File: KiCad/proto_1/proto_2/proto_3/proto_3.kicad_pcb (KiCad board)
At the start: 2 copper layers, 11 parts

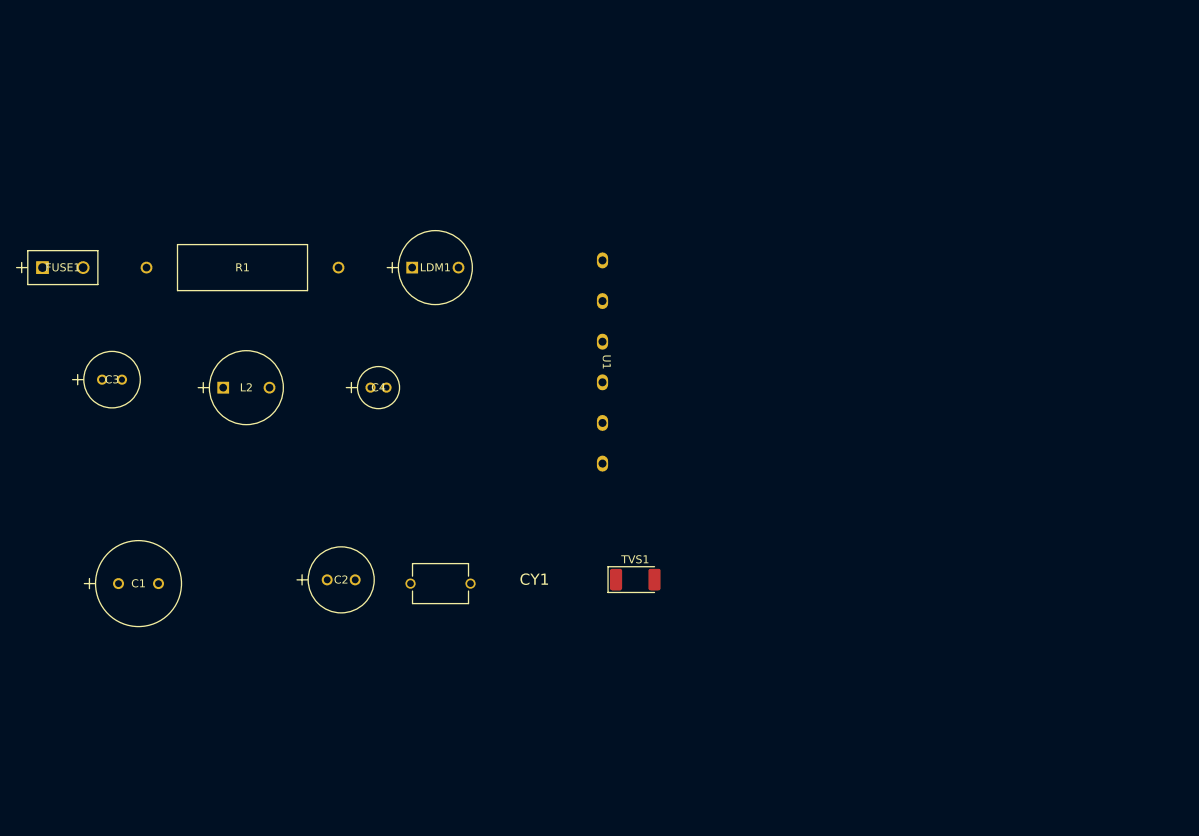
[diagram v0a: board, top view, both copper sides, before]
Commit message: Added through-holes for 120v source, moved components around on pcb
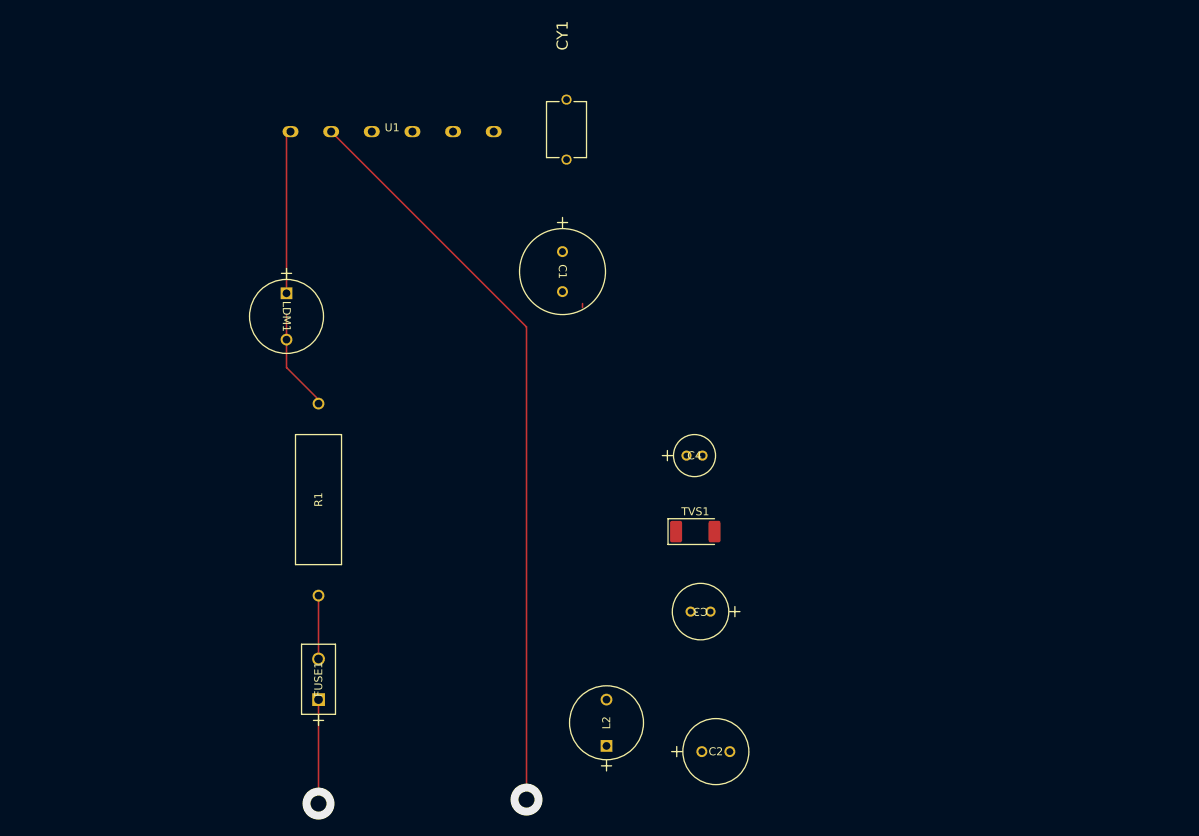
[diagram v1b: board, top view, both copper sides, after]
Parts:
- moved C3 81.4 mm to (157.5, 120.0), turned to 180 degrees
- moved C1 69.3 mm to (139.0, 75.0), turned to -90 degrees
- moved L2 65.6 mm to (144.5, 136.8), turned to 90 degrees
- moved FUSE1 64.1 mm to (108.5, 131.0), turned to 90 degrees
- moved CY1 58.9 mm to (139.5, 59.8), turned to 90 degrees
- moved C2 51.5 mm to (156.4, 137.5)
- moved R1 46.3 mm to (108.5, 118.0), turned to 90 degrees
- moved C4 40.4 mm to (154.5, 100.5)
- moved U1 39.0 mm to (117.7, 60.0), turned to 0 degrees
- moved LDM1 16.0 mm to (104.5, 80.2), turned to -90 degrees
- moved TVS1 9.60 mm to (155.6, 110.0)
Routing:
- net unconnected-(U1-AC(N)-Pad2): track 0.00 -> 93.6 mm, vias 0 -> 1
- net Net-(U1-AC(L)): track 0.00 -> 20.4 mm
- net unconnected-(FUSE1-Pad1): track 0.00 -> 13.0 mm, vias 0 -> 1
- net Net-(LDM1-Pad2): track 0.00 -> 12.7 mm
- net Net-(FUSE1-Pad2): track 0.00 -> 7.92 mm
- net (no net): track 0.00 -> 0.50 mm

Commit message: Changed transformer footprint, moved components on pcb
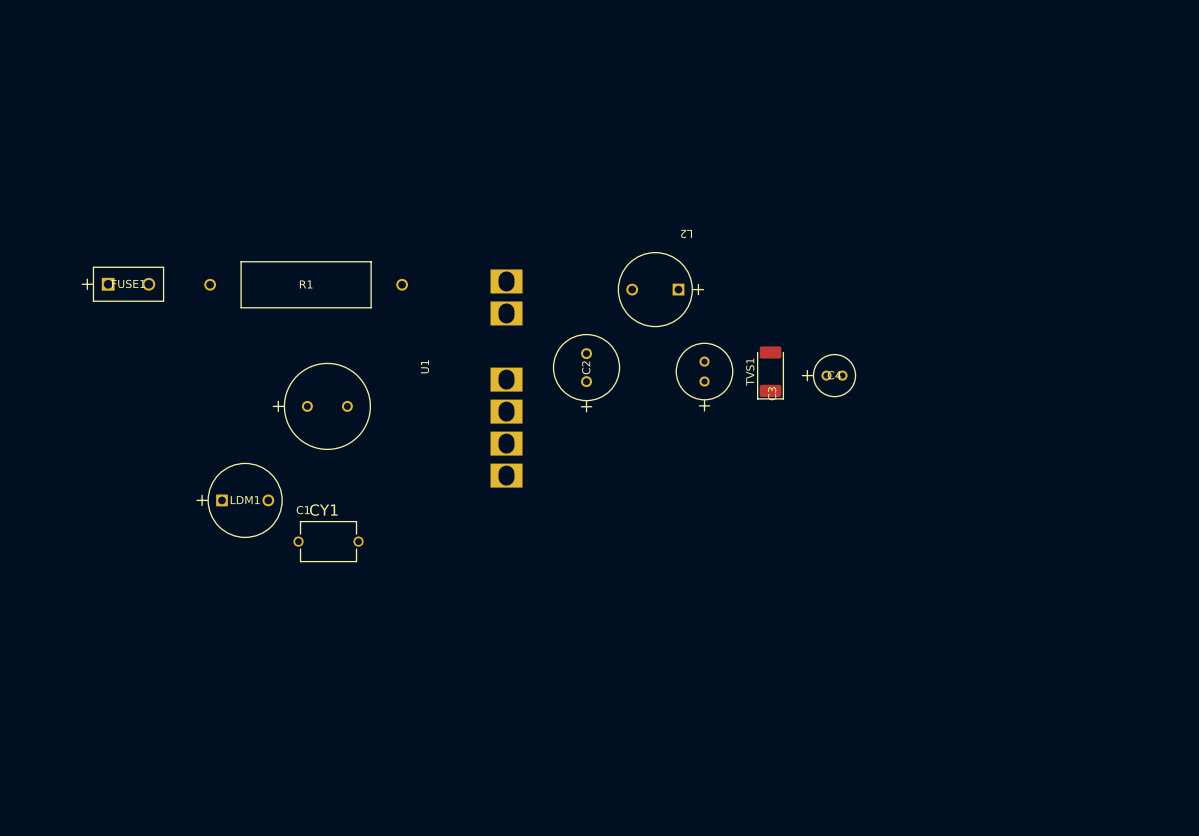
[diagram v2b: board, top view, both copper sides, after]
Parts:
- U1: footprint stuff:power -> stuff:transformer_MPL-05SC-F
- moved CY1 59.5 mm to (109.8, 111.2), turned to 0 degrees
- moved FUSE1 58.2 mm to (82.2, 79.1), turned to 0 degrees
- moved L2 57.7 mm to (153.5, 79.8), turned to 180 degrees
- moved C2 48.4 mm to (142.0, 91.2), turned to 90 degrees
- moved R1 41.1 mm to (95.0, 79.1), turned to 0 degrees
- moved C1 37.3 mm to (107.1, 94.4), turned to 0 degrees
- moved U1 32.7 mm to (132.0, 89.4), turned to 90 degrees
- moved C3 28.8 mm to (156.8, 91.2), turned to 90 degrees
- moved LDM1 27.1 mm to (96.4, 106.1), turned to 0 degrees
- moved TVS1 22.1 mm to (165.0, 90.0), turned to 90 degrees
- moved C4 20.2 mm to (172.0, 90.5)
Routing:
- net unconnected-(U1-AC(N)-Pad2): track 93.6 -> 0.00 mm, vias 1 -> 0
- net Net-(U1-AC(L)): track 20.4 -> 0.00 mm
- net unconnected-(FUSE1-Pad1): track 13.0 -> 0.00 mm, vias 1 -> 0
- net Net-(LDM1-Pad2): track 12.7 -> 0.00 mm
- net Net-(FUSE1-Pad2): track 7.92 -> 0.00 mm
- net (no net): track 0.50 -> 0.00 mm

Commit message: removed zips, added screw terminals, updated pcb layout
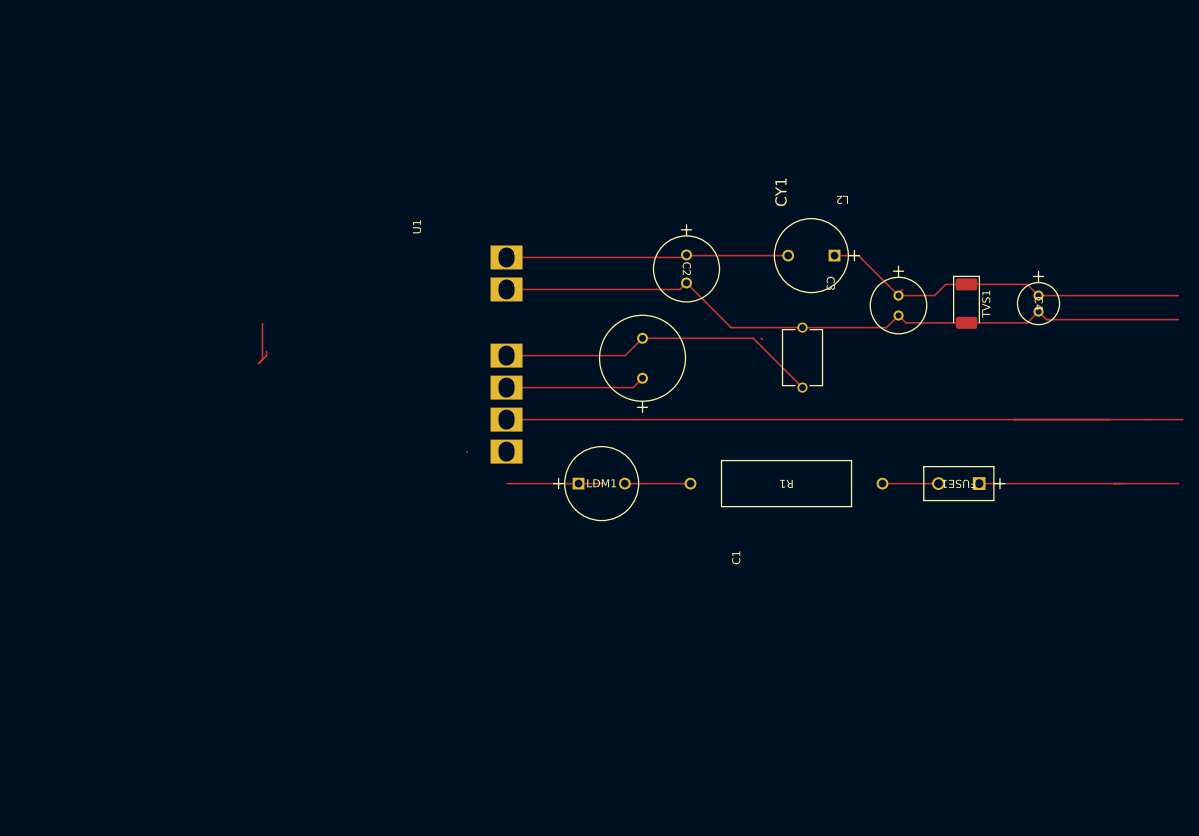
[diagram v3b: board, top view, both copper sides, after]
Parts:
- moved FUSE1 111.7 mm to (191.1, 104.0), turned to 180 degrees
- moved R1 87.6 mm to (179.0, 104.0), turned to 180 degrees
- moved CY1 63.6 mm to (169.0, 88.2), turned to 90 degrees
- moved LDM1 44.6 mm to (141.0, 104.0)
- moved C1 42.0 mm to (149.0, 90.8), turned to 90 degrees
- moved C4 28.3 mm to (198.5, 80.5), turned to -90 degrees
- moved C3 26.5 mm to (181.0, 80.5), turned to -90 degrees
- moved TVS1 25.9 mm to (189.5, 81.5), turned to -90 degrees
- moved C2 20.2 mm to (154.5, 75.4), turned to -90 degrees
- moved L2 20.0 mm to (173.0, 75.5)
- moved U1 3.00 mm to (132.0, 86.4)
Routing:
- net unconnected-(U1-AC(N)-Pad2): track 0.00 -> 96.5 mm
- net Net-(TVS1-A): track 0.00 -> 88.7 mm
- net Net-(TVS1-K): track 0.00 -> 46.8 mm
- net Net-(U1--V(cap)): track 0.00 -> 40.7 mm
- net Net-(U1-+Vo): track 0.00 -> 35.4 mm
- net unconnected-(FUSE1-Pad1): track 0.00 -> 26.0 mm
- net Net-(U1-+V(cap)): track 0.00 -> 17.5 mm
- net Net-(U1-AC(L)): track 0.00 -> 12.0 mm
- net Net-(LDM1-Pad2): track 0.00 -> 7.71 mm
- net (no net): track 0.00 -> 7.22 mm
- net Net-(FUSE1-Pad2): track 0.00 -> 7.00 mm

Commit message: added tvs diode and 4 port screw down block to schematic
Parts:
- removed TVS1: ~, Diode_SMD:D_MELF
- added CR1: DIODE, stuff:SMBJ7.0A, F.Cu at (162.0, 70.6)
- added J1: ~, stuff:screw_down_1x4, F.Cu at (192.0, 78.5)
- moved C1 32.0 mm to (119.0, 79.8)
- moved C2 32.0 mm to (124.5, 64.4)
- moved C3 32.0 mm to (151.0, 69.5)
- moved CY1 32.0 mm to (139.0, 77.2)
- moved FUSE1 32.0 mm to (161.1, 93.0)
- moved L2 32.0 mm to (143.0, 64.5)
- moved LDM1 32.0 mm to (111.0, 93.0)
- moved R1 32.0 mm to (149.0, 93.0)
- moved U1 32.0 mm to (102.0, 75.4)
- moved C4 25.0 mm to (175.0, 72.0)
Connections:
- FUSE1 pad 1: unconnected-(FUSE1-Pad1) -> Net-(FUSE1-Pad1)
- U1 pad 2: unconnected-(U1-AC(N)-Pad2) -> Net-(U1-AC(N))
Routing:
- net unconnected-(U1-AC(N)-Pad2): track 96.5 -> 0.00 mm
- net Net-(U1-AC(N)): track 0.00 -> 91.7 mm
- net Net-(FUSE1-Pad1): track 0.00 -> 33.8 mm
- net unconnected-(FUSE1-Pad1): track 26.0 -> 0.00 mm
- net Net-(C3-Pad1): track 46.8 -> 37.2 mm
- net (no net): track 7.22 -> 0.10 mm
- net Net-(U1--Vo): track 88.7 -> 93.1 mm

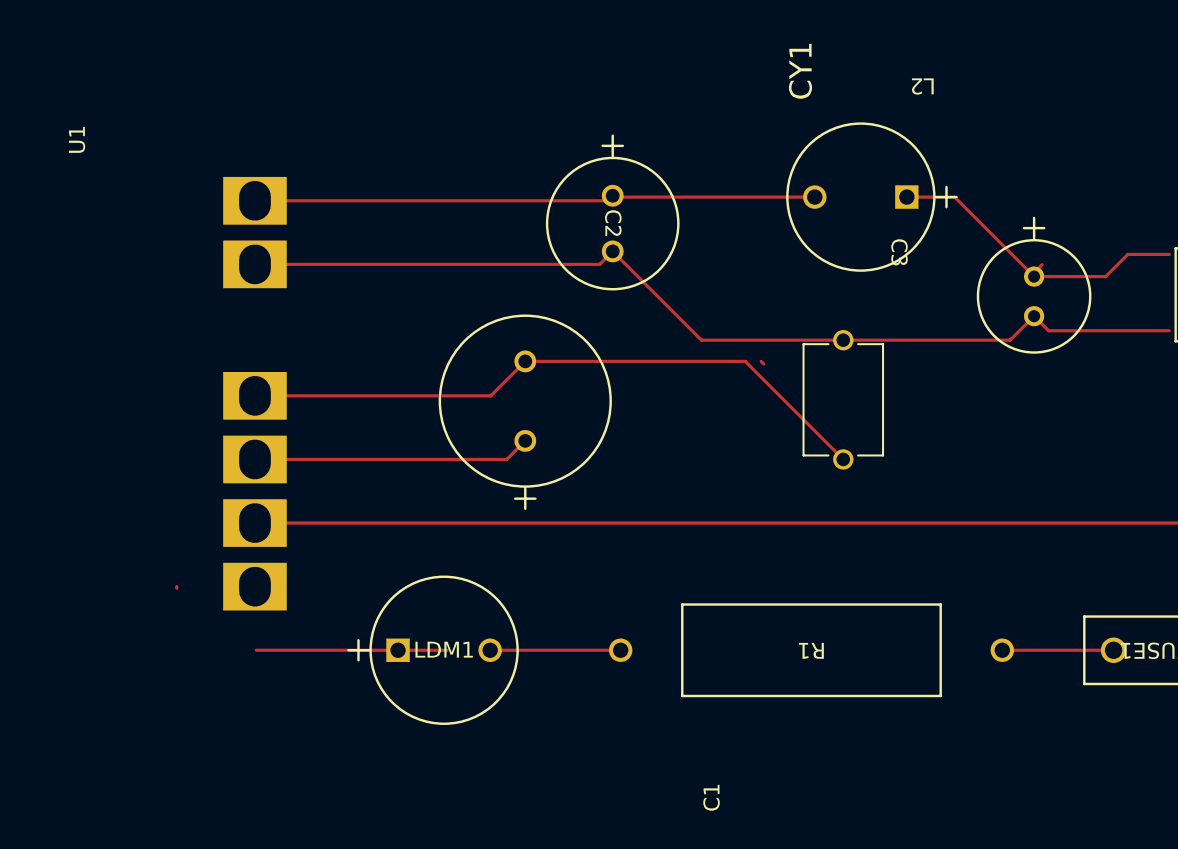
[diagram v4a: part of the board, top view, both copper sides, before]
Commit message: Added correct LDM inductor, footprint and symbol
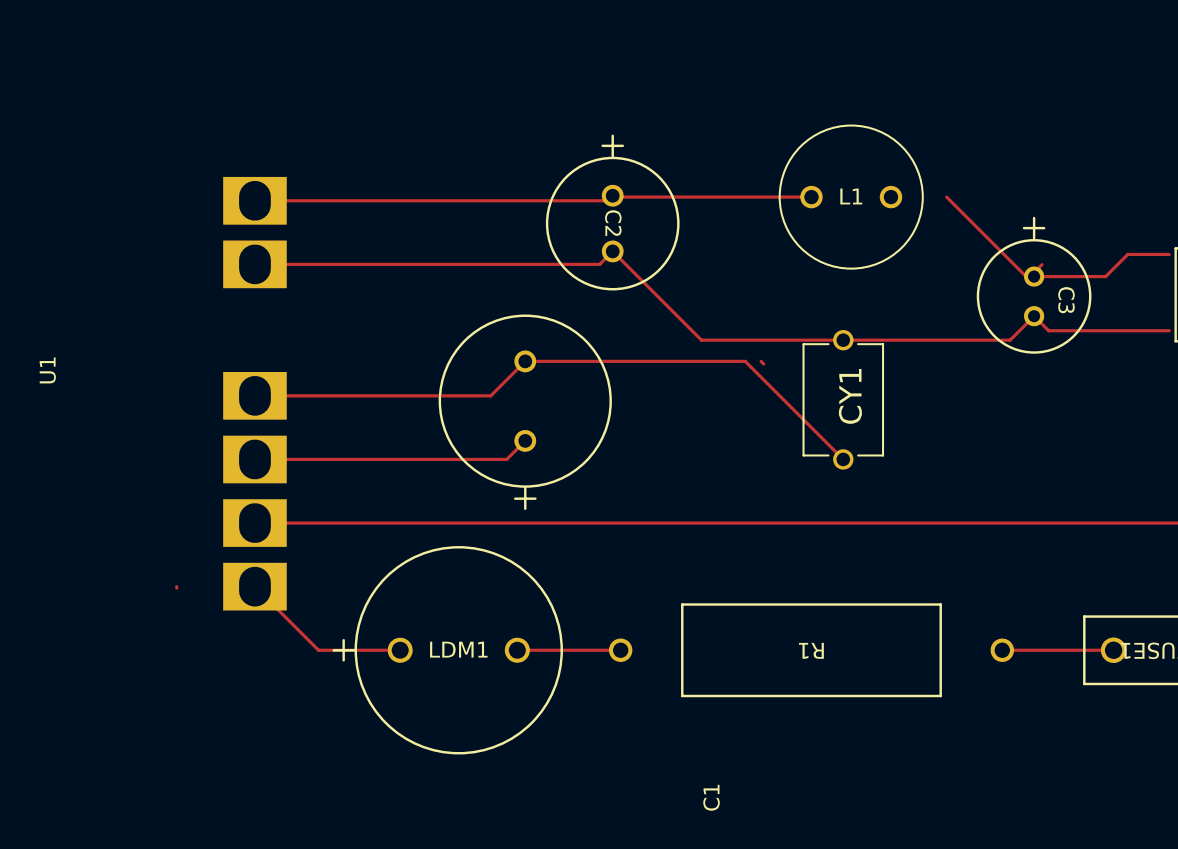
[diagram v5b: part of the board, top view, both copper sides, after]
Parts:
- removed L2: ~, Inductor-4.7uH-60ohm:IND_BOURNS_RLB9012
- added L1: RLB9012-4R7ML, stuff:IND_RLB9012-4R7ML, F.Cu at (139.5, 64.5)
- LDM1: footprint Inductor-4.7uH-60ohm:IND_BOURNS_RLB9012 -> stuff:AIUR-06_ABR
- moved LDM1 0.13 mm to (111.1, 93.0)
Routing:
- net Net-(C3-Pad1): track 37.2 -> 34.7 mm
- net Net-(U1-AC(L)): track 12.0 -> 10.8 mm
- net Net-(LDM1-Pad2): track 7.71 -> 6.50 mm

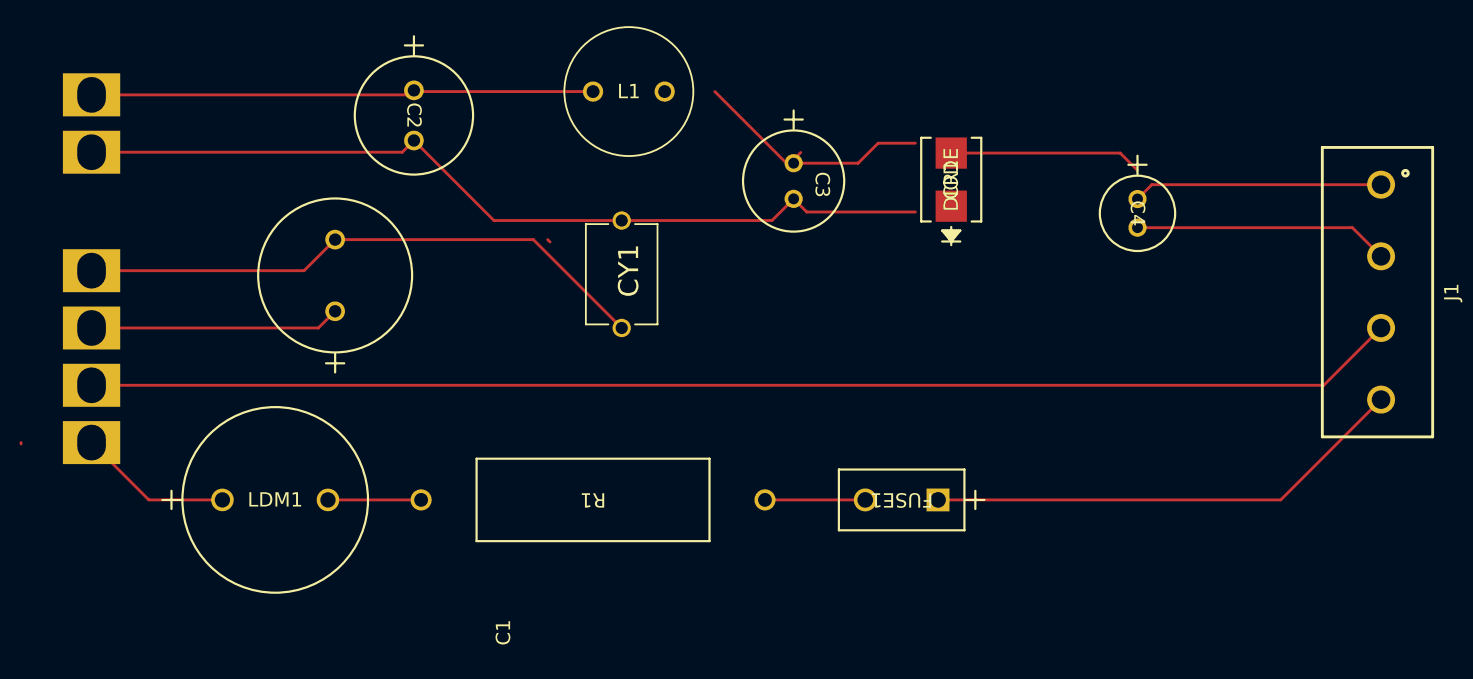
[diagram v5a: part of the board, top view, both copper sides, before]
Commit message: Added correct TVS diode footprint with correct polarities.
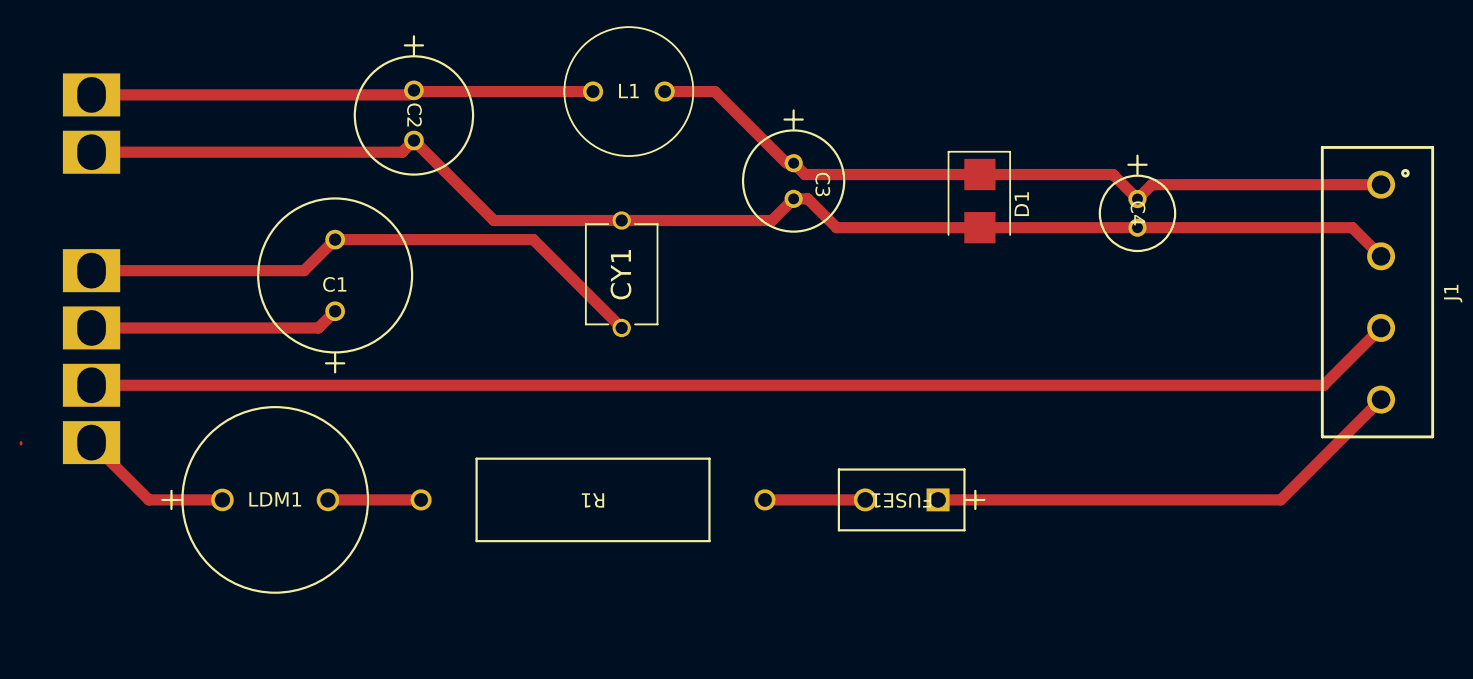
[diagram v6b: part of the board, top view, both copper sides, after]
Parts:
- removed CR1: DIODE, stuff:SMBJ7.0A
- added D1: SM6T6V8A, stuff:TVS_DIODE_NEW, F.Cu at (164.0, 72.4)
- L1: value RLB9012-4R7ML -> ~
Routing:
- net Net-(D1-A1): track 34.7 -> 53.8 mm
- net Net-(D1-A2): track 93.1 -> 94.9 mm
